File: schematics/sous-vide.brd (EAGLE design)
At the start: 160 x 100 mm, 27 parts, among them IC1 MEGA32-P, Q2 BC517, Q3 BC517

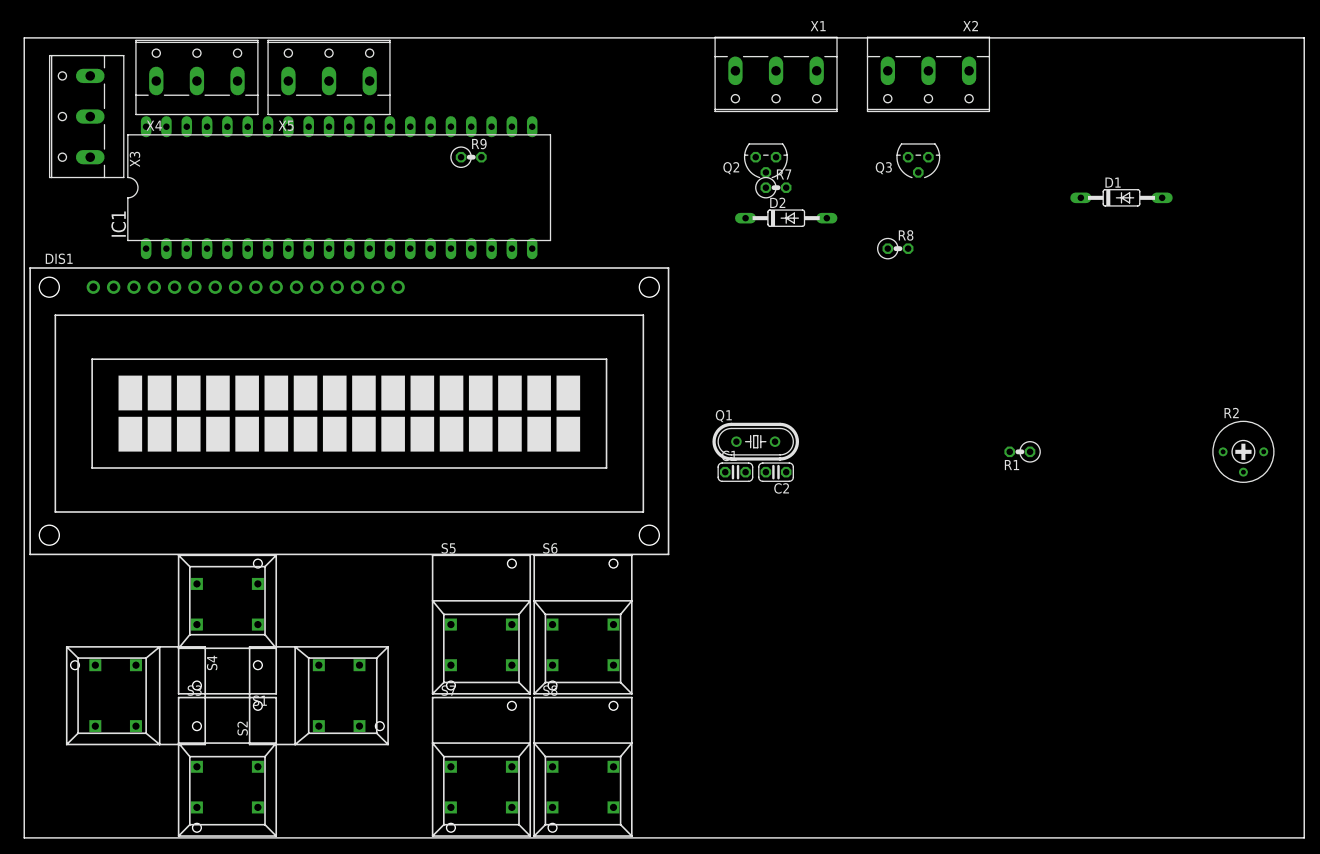
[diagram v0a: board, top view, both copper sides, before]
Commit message: Electronic schema and board updated
Created an 8x8 cm board for cpu, display and buttons.
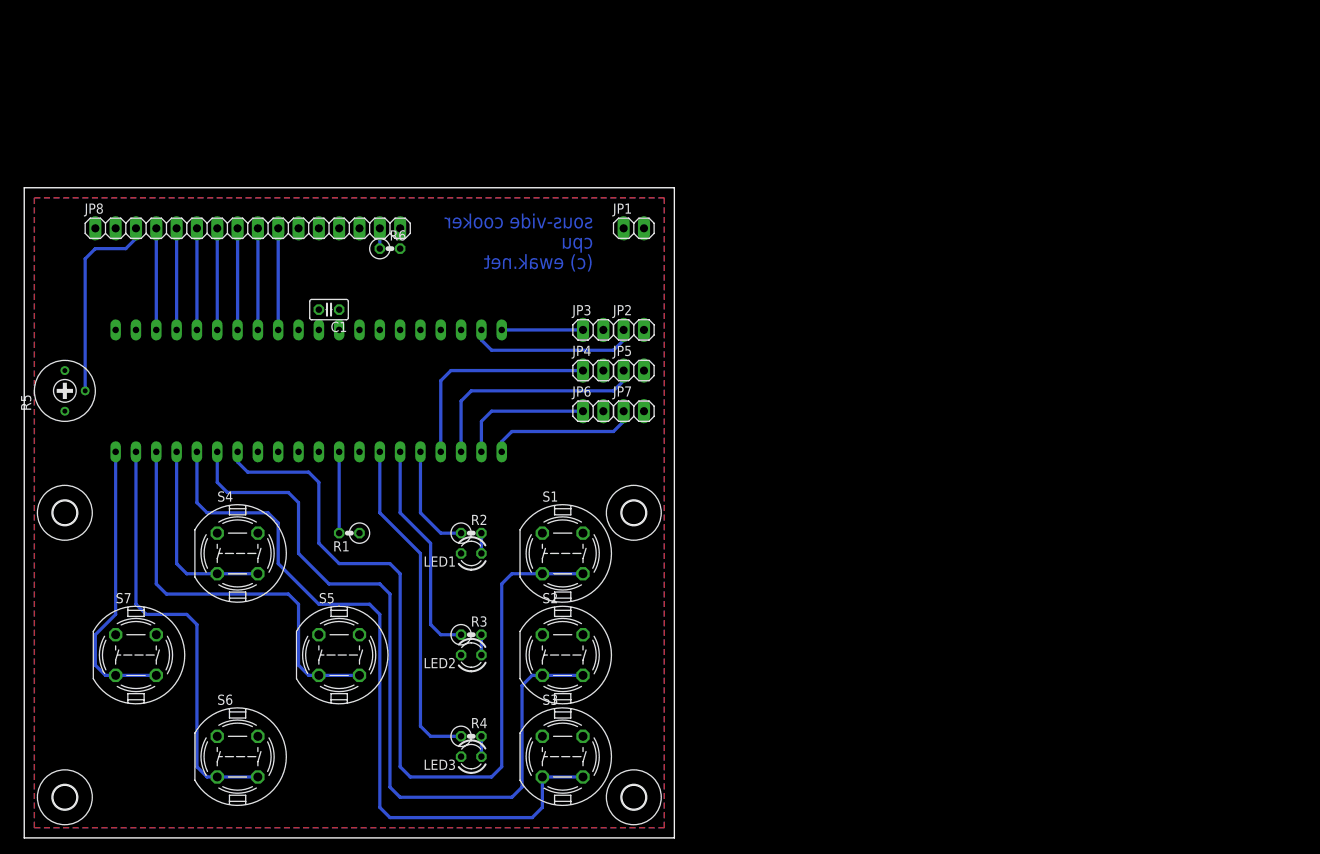
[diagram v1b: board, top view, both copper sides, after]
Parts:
- removed C2: (no value), rcl:C025-024X044
- removed D1, D2: 1N4148DO35-10, diode:DO35-10
- removed DIS1: TUXGR_16X2_R2, display-lcd:TUXGR_16X2_R2
- removed Q1: (no value), crystal:HC49/S
- removed Q2, Q3: BC517, transistor-npn:TO92
- removed R7, R8, R9: 100k, rcl:0207/2V
- removed S8: 5501, switch:5501
- removed X1, X2, X3, X4, X5: (no value), con-wago-508:W237-3E
- added H1, H2, H3, H4: MOUNT-HOLE3.0, holes:3,0
- added JP1: Power, pinhead:1X02
- added JP2, JP3: Sensor, pinhead:1X02
- added JP4, JP5: aux, pinhead:1X02
- added JP6: heater, pinhead:1X02
- added JP7: pump, pinhead:1X02
- added JP8: display, pinhead:1X16
- added LED1, LED2, LED3: (no value), led:LED3MM
- added R3, R4, R6: 330, rcl:0207/2V
- added R5: (no value), resistor:RTRIM3339P
- C1: device rcl:C025-024X044 -> resistor:C025-025X050
- R1: value 180 -> 100k
- R2: value (none) -> 330; device resistor:RTRIM3339P -> rcl:0207/2V
- S1, S2, S3, S4, S5, S6, S7: value 5501 -> DT6; device switch:5501 -> switch-misc:DT6
- moved R2 97.1 mm to (55.9, 38.1)
- moved R1 84.4 mm to (40.6, 38.1)
- moved C1 54.7 mm to (38.1, 66.0), turned to 180 degrees
- moved S6 46.2 mm to (26.7, 10.2), turned to 0 degrees
- moved S7 45.4 mm to (14.0, 22.9), turned to 0 degrees
- moved S1 42.8 mm to (67.3, 35.6), turned to 0 degrees
- moved S3 41.9 mm to (67.3, 10.2), turned to 0 degrees
- moved S2 30.9 mm to (67.3, 22.9)
- moved IC1 25.7 mm to (35.6, 55.9), flipped to the bottom
- moved S4 21.8 mm to (26.7, 35.6), turned to 0 degrees
- moved S5 18.2 mm to (39.4, 22.9), turned to 0 degrees
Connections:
- removed net SWITCH0: IC1.1, S1.1A, S1.1B
- removed net SWITCH1: IC1.2, S2.1A, S2.1B
- removed net SWITCH2: IC1.3, S3.1A, S3.1B
- removed net SWITCH3: IC1.4, S4.1A, S4.1B
- removed net SWITCH4: IC1.5, S5.1A, S5.1B
- removed net SWITCH5: IC1.6, S6.1A, S6.1B
- removed net SWITCH6: IC1.7, S7.1A, S7.1B
- removed net SWITCH7: IC1.8, S8.1A, S8.1B
- new net BUTTON0: IC1.14, S1.3, S1.4
- new net BUTTON1: IC1.15, S2.3, S2.4
- new net BUTTON2: IC1.16, S3.3, S3.4
- new net BUTTON3: IC1.17, S4.3, S4.4
- new net BUTTON4: IC1.18, S5.3, S5.4
- new net BUTTON5: IC1.19, S6.3, S6.4
- new net BUTTON6: IC1.20, S7.3, S7.4
- new net BUTTON7: IC1.21
- new net N$14: JP8.3, R5.2
- new net N$15: JP8.15, R6.1
- net DISPLAY0: now also IC1.22; no longer DIS1.4, IC1.14
- net DISPLAY1: now also IC1.23, JP8.4; no longer DIS1.5, IC1.15
- net DISPLAY2: now also IC1.24, JP8.5; no longer DIS1.6, IC1.16
- net DISPLAY3: now also IC1.25, JP8.6; no longer DIS1.11, IC1.17
- net DISPLAY4: now also IC1.26, JP8.7; no longer DIS1.12, IC1.18
- net DISPLAY5: now also IC1.27, JP8.8; no longer DIS1.13, IC1.19
- net DISPLAY6: now also IC1.28, JP8.9; no longer DIS1.14, IC1.20
- net DISPLAY7: now also IC1.29, JP8.10; no longer IC1.21
- net GND: now also JP1.2, JP2.2, JP3.2, JP4.2, JP5.2, JP6.2, JP7.2, JP8.1, JP8.16, LED1.K, LED2.K, LED3.K, R5.3, S1.1, S1.2, S2.1, S2.2, S3.1, S3.2, S4.1, S4.2, S5.1, S5.2, S6.1, S6.2, S7.1, S7.2; no longer C2.2, DIS1.1, Q2.1, Q3.1, R1.2, R2.1, S1.NO, S2.NO, S3.NO, S4.NO, S5.NO, S6.NO, S7.NO, S8.NO, X1.3, X2.3, X3.3, X4.3, X5.3
- net N$1: now also IC1.1, JP7.1; no longer C1.1, IC1.12, Q1.1
- net N$10: now also IC1.5, R2.1; no longer Q3.2, R8.2
- net N$11: now also IC1.6, R3.1; no longer IC1.39, X3.2
- net N$12: now also JP3.1; no longer X4.2
- net N$13: now also IC1.7, R4.1; no longer DIS1.3, R2.2
- net N$2: now also IC1.2, JP6.1; no longer C2.1, IC1.13, Q1.2
- net N$3: now also R1.2; no longer R9.2
- net N$4: now also IC1.3, JP5.1; no longer D2.A, Q3.3, X2.2
- net N$5: now also IC1.4, JP4.1; no longer DIS1.16, R1.1
- net N$6: now also IC1.39, JP2.1; no longer IC1.22, R8.1
- net N$7: now also LED3.A, R4.2; no longer IC1.23, R7.1
- net N$8: now also LED2.A, R3.2; no longer Q2.2, R7.2
- net N$9: now also LED1.A, R2.2; no longer D1.A, Q2.3, X1.2
- net VCC: now also C1.1, JP1.1, JP8.2, R1.1, R5.1, R6.2; no longer D1.C, D2.C, DIS1.15, DIS1.2, R2.3, R9.1, X1.1, X2.1, X3.1, X4.1, X5.1
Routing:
- net BUTTON0: track 0.00 -> 103.3 mm
- net BUTTON1: track 0.00 -> 97.4 mm
- net BUTTON2: track 0.00 -> 92.4 mm
- net BUTTON5: track 0.00 -> 53.6 mm
- net BUTTON4: track 0.00 -> 51.1 mm
- net N$13: track 0.00 -> 42.0 mm
- net BUTTON6: track 0.00 -> 35.9 mm
- net N$4: track 0.00 -> 29.0 mm
- net N$11: track 0.00 -> 27.5 mm
- net N$5: track 0.00 -> 27.2 mm
- net N$14: track 0.00 -> 25.2 mm
- net BUTTON3: track 0.00 -> 24.7 mm
- net N$6: track 0.00 -> 21.4 mm
- net N$1: track 0.00 -> 18.8 mm
- net N$2: track 0.00 -> 17.0 mm
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- added copper zone on layer 16, net GND
- added copper zone on layer 1, net VCC
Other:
- board size 160 x 100 mm -> 81.3 x 81.3 mm
- board text added: "(c) ewak.net"
- board text added: "cpu"
- board text added: "sous-vide cooker"

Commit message: Optimized PCB
Optimized PCB with easier traces for buttons.
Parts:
- moved R3 2.54 mm to (55.9, 27.9)
- moved R4 2.54 mm to (55.9, 15.2)
- moved R2 2.54 mm to (55.9, 40.6)
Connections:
- net BUTTON3: now also S4.1, S4.2; no longer S4.3, S4.4
- net BUTTON4: now also S5.1, S5.2; no longer S5.3, S5.4
- net BUTTON5: now also S6.1, S6.2; no longer S6.3, S6.4
- net BUTTON6: now also S7.1, S7.2; no longer S7.3, S7.4
- net GND: now also S4.3, S4.4, S5.3, S5.4, S6.3, S6.4, S7.3, S7.4; no longer S4.1, S4.2, S5.1, S5.2, S6.1, S6.2, S7.1, S7.2
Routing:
- net BUTTON6: track 35.9 -> 27.9 mm
- net BUTTON5: track 53.6 -> 48.6 mm
- net BUTTON4: track 51.1 -> 46.0 mm
- net BUTTON3: track 24.7 -> 19.6 mm
- net N$11: track 27.5 -> 24.2 mm
- net N$13: track 42.0 -> 39.5 mm
- net N$8: track 2.54 -> 5.08 mm
- net N$7: track 2.54 -> 5.08 mm
- net N$9: track 2.54 -> 5.08 mm
- net N$10: track 13.8 -> 12.0 mm
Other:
- board text added: "+"
- board text added: "0"
- board text added: "cpu board"
- board text added: "ewak.net"
- board text removed: "(c) ewak.net"
- board text removed: "cpu"
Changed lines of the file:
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@@
 <wire x1="0" y1="81.27" x2="0" y2="0" width="0" layer="20"/>
 <text x="71.12" y="76.2" size="1.778" layer="16" rot="MR0">sous-vide cooker</text>
-<text x="71.12" y="71.12" size="1.778" layer="16" rot="MR0">(c) ewak.net</text>
-<text x="71.12" y="73.66" size="1.778" layer="16" rot="MR0">cpu</text>
+<text x="71.12" y="71.12" size="1.778" layer="16" rot="MR0">ewak.net</text>
+<text x="71.12" y="73.66" size="1.778" layer="16" rot="MR0">cpu board</text>
+<text x="78.105" y="72.39" size="1.778" layer="16" rot="MR0">0</text>
+<text x="75.565" y="72.39" size="1.778" layer="16" rot="MR0">+</text>
 </plain>
 <attributes>
@@
 <element name="JP4" library="pinhead" package="1X02" value="aux" x="71.12" y="58.42"/>
 <element name="JP2" library="pinhead" package="1X02" value="Sensor" x="76.2" y="63.5"/>
-<element name="R2" library="rcl" package="0207/2V" value="330" x="55.88" y="38.1"/>
-<element name="R3" library="rcl" package="0207/2V" value="330" x="55.88" y="25.4"/>
-<element name="R4" library="rcl" package="0207/2V" value="330" x="55.88" y="12.7"/>
+<element name="R2" library="rcl" package="0207/2V" value="330" x="55.88" y="40.64"/>
+<element name="R3" library="rcl" package="0207/2V" value="330" x="55.88" y="27.94"/>
+<element name="R4" library="rcl" package="0207/2V" value="330" x="55.88" y="15.24"/>
 <element name="C1" library="resistor" package="C025-025X050" value="" x="38.1" y="66.04" rot="R180"/>
 <element name="R5" library="resistor" package="RTRIM3339P" value="" x="5.08" y="55.88" rot="R90"/>
@@
 <contactref element="S2" pad="1"/>
 <contactref element="S3" pad="1"/>
-<contactref element="S4" pad="1"/>
-<contactref element="S5" pad="1"/>
-<contactref element="S6" pad="1"/>
-<contactref element="S7" pad="1"/>
-<contactref element="S5" pad="2"/>
-<contactref element="S6" pad="2"/>
-<contactref element="S7" pad="2"/>
-<contactref element="S4" pad="2"/>
 <contactref element="S3" pad="2"/>
 <contactref element="S1" pad="2"/>
@@
 <vertex x="80.01" y="80.01"/>
 </polygon>
+<contactref element="S4" pad="3"/>
+<contactref element="S7" pad="3"/>
+<contactref element="S5" pad="3"/>
+<contactref element="S6" pad="3"/>
+<contactref element="S5" pad="4"/>
+<contactref element="S6" pad="4"/>
+<contactref element="S7" pad="4"/>
+<contactref element="S4" pad="4"/>
 </signal>
 <signal name="N$3">
@@
 <signal name="BUTTON5">
 <contactref element="IC1" pad="19"/>
-<contactref element="S6" pad="3"/>
-<contactref element="S6" pad="4"/>
+<contactref element="S6" pad="2"/>
+<contactref element="S6" pad="1"/>
 <wire x1="13.97" y1="48.26" x2="13.97" y2="29.21" width="0.4064" layer="16"/>
 <wire x1="13.97" y1="29.21" x2="15.24" y2="27.94" width="0.4064" layer="16"/>
 <wire x1="15.24" y1="27.94" x2="20.32" y2="27.94" width="0.4064" layer="16"/>
 <wire x1="20.32" y1="27.94" x2="21.59" y2="26.67" width="0.4064" layer="16"/>
-<wire x1="21.59" y1="26.67" x2="21.59" y2="8.89" width="0.4064" layer="16"/>
-<wire x1="21.59" y1="8.89" x2="22.86" y2="7.62" width="0.4064" layer="16"/>
-<wire x1="22.86" y1="7.62" x2="24.13" y2="7.62" width="0.4064" layer="16"/>
-<wire x1="24.13" y1="7.62" x2="29.21" y2="7.62" width="0.4064" layer="16"/>
+<wire x1="21.59" y1="26.67" x2="21.59" y2="13.97" width="0.4064" layer="16"/>
+<wire x1="21.59" y1="13.97" x2="22.86" y2="12.7" width="0.4064" layer="16"/>
+<wire x1="22.86" y1="12.7" x2="24.13" y2="12.7" width="0.4064" layer="16"/>
+<wire x1="24.13" y1="12.7" x2="29.21" y2="12.7" width="0.4064" layer="16"/>
 </signal>
 <signal name="BUTTON6">
 <contactref element="IC1" pad="20"/>
-<contactref element="S7" pad="3"/>
-<contactref element="S7" pad="4"/>
-<wire x1="8.89" y1="21.59" x2="10.16" y2="20.32" width="0.4064" layer="16"/>
-<wire x1="10.16" y1="20.32" x2="11.43" y2="20.32" width="0.4064" layer="16"/>
-<wire x1="11.43" y1="20.32" x2="16.51" y2="20.32" width="0.4064" layer="16"/>
-<wire x1="8.89" y1="21.59" x2="8.89" y2="25.4" width="0.4064" layer="16"/>
-<wire x1="8.89" y1="25.4" x2="11.43" y2="27.94" width="0.4064" layer="16"/>
-<wire x1="11.43" y1="27.94" x2="11.43" y2="48.26" width="0.4064" layer="16"/>
+<contactref element="S7" pad="2"/>
+<contactref element="S7" pad="1"/>
+<wire x1="11.43" y1="48.26" x2="11.43" y2="25.4" width="0.4064" layer="16"/>
+<wire x1="11.43" y1="25.4" x2="16.51" y2="25.4" width="0.4064" layer="16"/>
 </signal>
 <signal name="BUTTON7">
@@
 <signal name="BUTTON4">
 <contactref element="IC1" pad="18"/>
-<contactref element="S5" pad="4"/>
-<contactref element="S5" pad="3"/>
+<contactref element="S5" pad="2"/>
+<contactref element="S5" pad="1"/>
 <wire x1="16.51" y1="48.26" x2="16.51" y2="31.75" width="0.4064" layer="16"/>
 <wire x1="16.51" y1="31.75" x2="17.78" y2="30.48" width="0.4064" layer="16"/>
 <wire x1="17.78" y1="30.48" x2="33.02" y2="30.48" width="0.4064" layer="16"/>
 <wire x1="33.02" y1="30.48" x2="34.29" y2="29.21" width="0.4064" layer="16"/>
-<wire x1="34.29" y1="29.21" x2="34.29" y2="21.59" width="0.4064" layer="16"/>
-<wire x1="34.29" y1="21.59" x2="35.56" y2="20.32" width="0.4064" layer="16"/>
-<wire x1="35.56" y1="20.32" x2="36.83" y2="20.32" width="0.4064" layer="16"/>
-<wire x1="36.83" y1="20.32" x2="41.91" y2="20.32" width="0.4064" layer="16"/>
+<wire x1="34.29" y1="29.21" x2="34.29" y2="26.67" width="0.4064" layer="16"/>
+<wire x1="34.29" y1="26.67" x2="35.56" y2="25.4" width="0.4064" layer="16"/>
+<wire x1="35.56" y1="25.4" x2="36.83" y2="25.4" width="0.4064" layer="16"/>
+<wire x1="36.83" y1="25.4" x2="41.91" y2="25.4" width="0.4064" layer="16"/>
 </signal>
 <signal name="BUTTON3">
 <contactref element="IC1" pad="17"/>
-<contactref element="S4" pad="3"/>
-<contactref element="S4" pad="4"/>
-<wire x1="29.21" y1="33.02" x2="20.32" y2="33.02" width="0.4064" layer="16"/>
-<wire x1="20.32" y1="33.02" x2="19.05" y2="34.29" width="0.4064" layer="16"/>
-<wire x1="19.05" y1="34.29" x2="19.05" y2="48.26" width="0.4064" layer="16"/>
-<wire x1="20.32" y1="33.02" x2="24.13" y2="33.02" width="0" layer="19" extent="16-16"/>
+<contactref element="S4" pad="2"/>
+<contactref element="S4" pad="1"/>
+<wire x1="19.05" y1="48.26" x2="19.05" y2="39.37" width="0.4064" layer="16"/>
+<wire x1="19.05" y1="39.37" x2="20.32" y2="38.1" width="0.4064" layer="16"/>
+<wire x1="20.32" y1="38.1" x2="29.21" y2="38.1" width="0.4064" layer="16"/>
+<wire x1="20.32" y1="38.1" x2="24.13" y2="38.1" width="0" layer="19" extent="16-16"/>
 </signal>
 <signal name="BUTTON1">
@@
 <contactref element="LED3" pad="A"/>
 <contactref element="R4" pad="2"/>
-<wire x1="57.15" y1="12.7" x2="57.15" y2="10.16" width="0.4064" layer="16"/>
+<wire x1="57.15" y1="15.24" x2="57.15" y2="10.16" width="0.4064" layer="16"/>
 </signal>
 <signal name="N$8">
 <contactref element="LED2" pad="A"/>
 <contactref element="R3" pad="2"/>
-<wire x1="57.15" y1="22.86" x2="57.15" y2="25.4" width="0.4064" layer="16"/>
+<wire x1="57.15" y1="22.86" x2="57.15" y2="27.94" width="0.4064" layer="16"/>
 </signal>
 <signal name="N$9">
 <contactref element="LED1" pad="A"/>
 <contactref element="R2" pad="2"/>
-<wire x1="57.15" y1="35.56" x2="57.15" y2="38.1" width="0.4064" layer="16"/>
+<wire x1="57.15" y1="35.56" x2="57.15" y2="40.64" width="0.4064" layer="16"/>
 </signal>
 <signal name="N$10">
 <contactref element="R2" pad="1"/>
 <contactref element="IC1" pad="5"/>
-<wire x1="54.61" y1="38.1" x2="52.07" y2="38.1" width="0.4064" layer="16"/>
-<wire x1="52.07" y1="38.1" x2="49.53" y2="40.64" width="0.4064" layer="16"/>
-<wire x1="49.53" y1="40.64" x2="49.53" y2="48.26" width="0.4064" layer="16"/>
+<wire x1="54.61" y1="40.64" x2="50.8" y2="40.64" width="0.4064" layer="16"/>
+<wire x1="49.53" y1="41.91" x2="49.53" y2="48.26" width="0.4064" layer="16"/>
+<wire x1="49.53" y1="41.91" x2="50.8" y2="40.64" width="0.4064" layer="16"/>
 </signal>
 <signal name="N$11">
 <contactref element="IC1" pad="6"/>
 <contactref element="R3" pad="1"/>
-<wire x1="54.61" y1="25.4" x2="52.07" y2="25.4" width="0.4064" layer="16"/>
-<wire x1="52.07" y1="25.4" x2="50.8" y2="26.67" width="0.4064" layer="16"/>
-<wire x1="50.8" y1="26.67" x2="50.8" y2="36.83" width="0.4064" layer="16"/>
-<wire x1="50.8" y1="36.83" x2="46.99" y2="40.64" width="0.4064" layer="16"/>
+<wire x1="54.61" y1="27.94" x2="53.34" y2="27.94" width="0.4064" layer="16"/>
+<wire x1="53.34" y1="27.94" x2="52.07" y2="29.21" width="0.4064" layer="16"/>
+<wire x1="52.07" y1="29.21" x2="52.07" y2="35.56" width="0.4064" layer="16"/>
+<wire x1="52.07" y1="35.56" x2="46.99" y2="40.64" width="0.4064" layer="16"/>
 <wire x1="46.99" y1="40.64" x2="46.99" y2="48.26" width="0.4064" layer="16"/>
 </signal>
@@
 <contactref element="R4" pad="1"/>
 <contactref element="IC1" pad="7"/>
-<wire x1="54.61" y1="12.7" x2="50.8" y2="12.7" width="0.4064" layer="16"/>
-<wire x1="50.8" y1="12.7" x2="49.53" y2="13.97" width="0.4064" layer="16"/>
-<wire x1="49.53" y1="13.97" x2="49.53" y2="35.56" width="0.4064" layer="16"/>
-<wire x1="44.45" y1="48.26" x2="44.45" y2="40.64" width="0.4064" layer="16"/>
-<wire x1="44.45" y1="40.64" x2="49.53" y2="35.56" width="0.4064" layer="16"/>
+<wire x1="54.61" y1="15.24" x2="50.8" y2="15.24" width="0.4064" layer="16"/>
+<wire x1="50.8" y1="15.24" x2="49.53" y2="16.51" width="0.4064" layer="16"/>
+<wire x1="49.53" y1="16.51" x2="49.53" y2="34.29" width="0.4064" layer="16"/>
+<wire x1="44.45" y1="48.26" x2="44.45" y2="39.37" width="0.4064" layer="16"/>
+<wire x1="44.45" y1="39.37" x2="49.53" y2="34.29" width="0.4064" layer="16"/>
 </signal>
 <signal name="N$14">

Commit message: initial steps to move from at32u4 naar at32
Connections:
- net DISPLAY4: now also JP8.11; no longer JP8.7
- net DISPLAY5: now also JP8.12; no longer JP8.8
- net DISPLAY6: now also JP8.13; no longer JP8.9
- net DISPLAY7: now also JP8.14; no longer JP8.10
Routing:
- net DISPLAY4: track 12.7 -> 21.4 mm
- net DISPLAY7: track 12.7 -> 21.4 mm
- net DISPLAY6: track 12.7 -> 21.4 mm
- net DISPLAY5: track 12.7 -> 21.4 mm
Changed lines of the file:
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@@
 <signal name="DISPLAY4">
 <contactref element="IC1" pad="26"/>
-<contactref element="JP8" pad="7"/>
-<wire x1="24.13" y1="76.2" x2="24.13" y2="63.5" width="0.4064" layer="16"/>
+<contactref element="JP8" pad="11"/>
+<wire x1="24.13" y1="63.5" x2="24.13" y2="71.12" width="0.4064" layer="16"/>
+<wire x1="24.13" y1="71.12" x2="25.4" y2="72.39" width="0.4064" layer="16"/>
+<wire x1="25.4" y1="72.39" x2="33.02" y2="72.39" width="0.4064" layer="16"/>
+<wire x1="33.02" y1="72.39" x2="34.29" y2="73.66" width="0.4064" layer="16"/>
+<wire x1="34.29" y1="73.66" x2="34.29" y2="76.2" width="0.4064" layer="16"/>
 </signal>
 <signal name="DISPLAY5">
 <contactref element="IC1" pad="27"/>
-<contactref element="JP8" pad="8"/>
-<wire x1="26.67" y1="63.5" x2="26.67" y2="76.2" width="0.4064" layer="16"/>
+<contactref element="JP8" pad="12"/>
+<wire x1="26.67" y1="63.5" x2="26.67" y2="69.85" width="0.4064" layer="16"/>
+<wire x1="26.67" y1="69.85" x2="27.94" y2="71.12" width="0.4064" layer="16"/>
+<wire x1="27.94" y1="71.12" x2="35.56" y2="71.12" width="0.4064" layer="16"/>
+<wire x1="35.56" y1="71.12" x2="36.83" y2="72.39" width="0.4064" layer="16"/>
+<wire x1="36.83" y1="72.39" x2="36.83" y2="76.2" width="0.4064" layer="16"/>
 </signal>
 <signal name="DISPLAY6">
 <contactref element="IC1" pad="28"/>
-<contactref element="JP8" pad="9"/>
-<wire x1="29.21" y1="63.5" x2="29.21" y2="76.2" width="0.4064" layer="16"/>
+<contactref element="JP8" pad="13"/>
+<wire x1="29.21" y1="63.5" x2="29.21" y2="68.58" width="0.4064" layer="16"/>
+<wire x1="29.21" y1="68.58" x2="30.48" y2="69.85" width="0.4064" layer="16"/>
+<wire x1="30.48" y1="69.85" x2="38.1" y2="69.85" width="0.4064" layer="16"/>
+<wire x1="38.1" y1="69.85" x2="39.37" y2="71.12" width="0.4064" layer="16"/>
+<wire x1="39.37" y1="71.12" x2="39.37" y2="76.2" width="0.4064" layer="16"/>
 </signal>
 <signal name="DISPLAY7">
 <contactref element="IC1" pad="29"/>
-<contactref element="JP8" pad="10"/>
-<wire x1="31.75" y1="76.2" x2="31.75" y2="63.5" width="0.4064" layer="16"/>
+<contactref element="JP8" pad="14"/>
+<wire x1="31.75" y1="63.5" x2="31.75" y2="67.31" width="0.4064" layer="16"/>
+<wire x1="31.75" y1="67.31" x2="33.02" y2="68.58" width="0.4064" layer="16"/>
+<wire x1="33.02" y1="68.58" x2="40.64" y2="68.58" width="0.4064" layer="16"/>
+<wire x1="40.64" y1="68.58" x2="41.91" y2="69.85" width="0.4064" layer="16"/>
+<wire x1="41.91" y1="69.85" x2="41.91" y2="76.2" width="0.4064" layer="16"/>
 </signal>
 <signal name="BUTTON5">
